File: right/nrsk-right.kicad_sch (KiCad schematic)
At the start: 138 parts, among them J1 USB-C, J2 USB-C, J3 OLED 128x32, SW1 71, SW10 8, SW11 9, SW12 0, SW13 -, SW14 =, SW15 Backspace, SW16 75, SW17 Y, SW18 U, SW19 I, SW2 F7, SW20 O, SW21 P, SW22 [, SW23 ], SW24 \, SW25 77, SW26 H, SW27 J, SW28 K, SW29 L, SW3 F8, SW30 ;, SW31 ', SW32 Enter, SW33 79, SW34 N, SW35 M, SW36 ,, SW37 ., SW38 /, SW39 ↑, SW4 F9, SW40 fn, SW41 81, SW42 Space, SW43 Space, SW44 Cmd, SW45 Opt, SW46 ←, SW47 ↓, SW48 →, SW5 F10, SW6 F11, SW7 F12, SW8 73, SW9 7, U1 RP2040, U2 USBLC6-2SC6, U4 AP2112K-3.3, U5 W25Q128JVS, Y1 12MHz

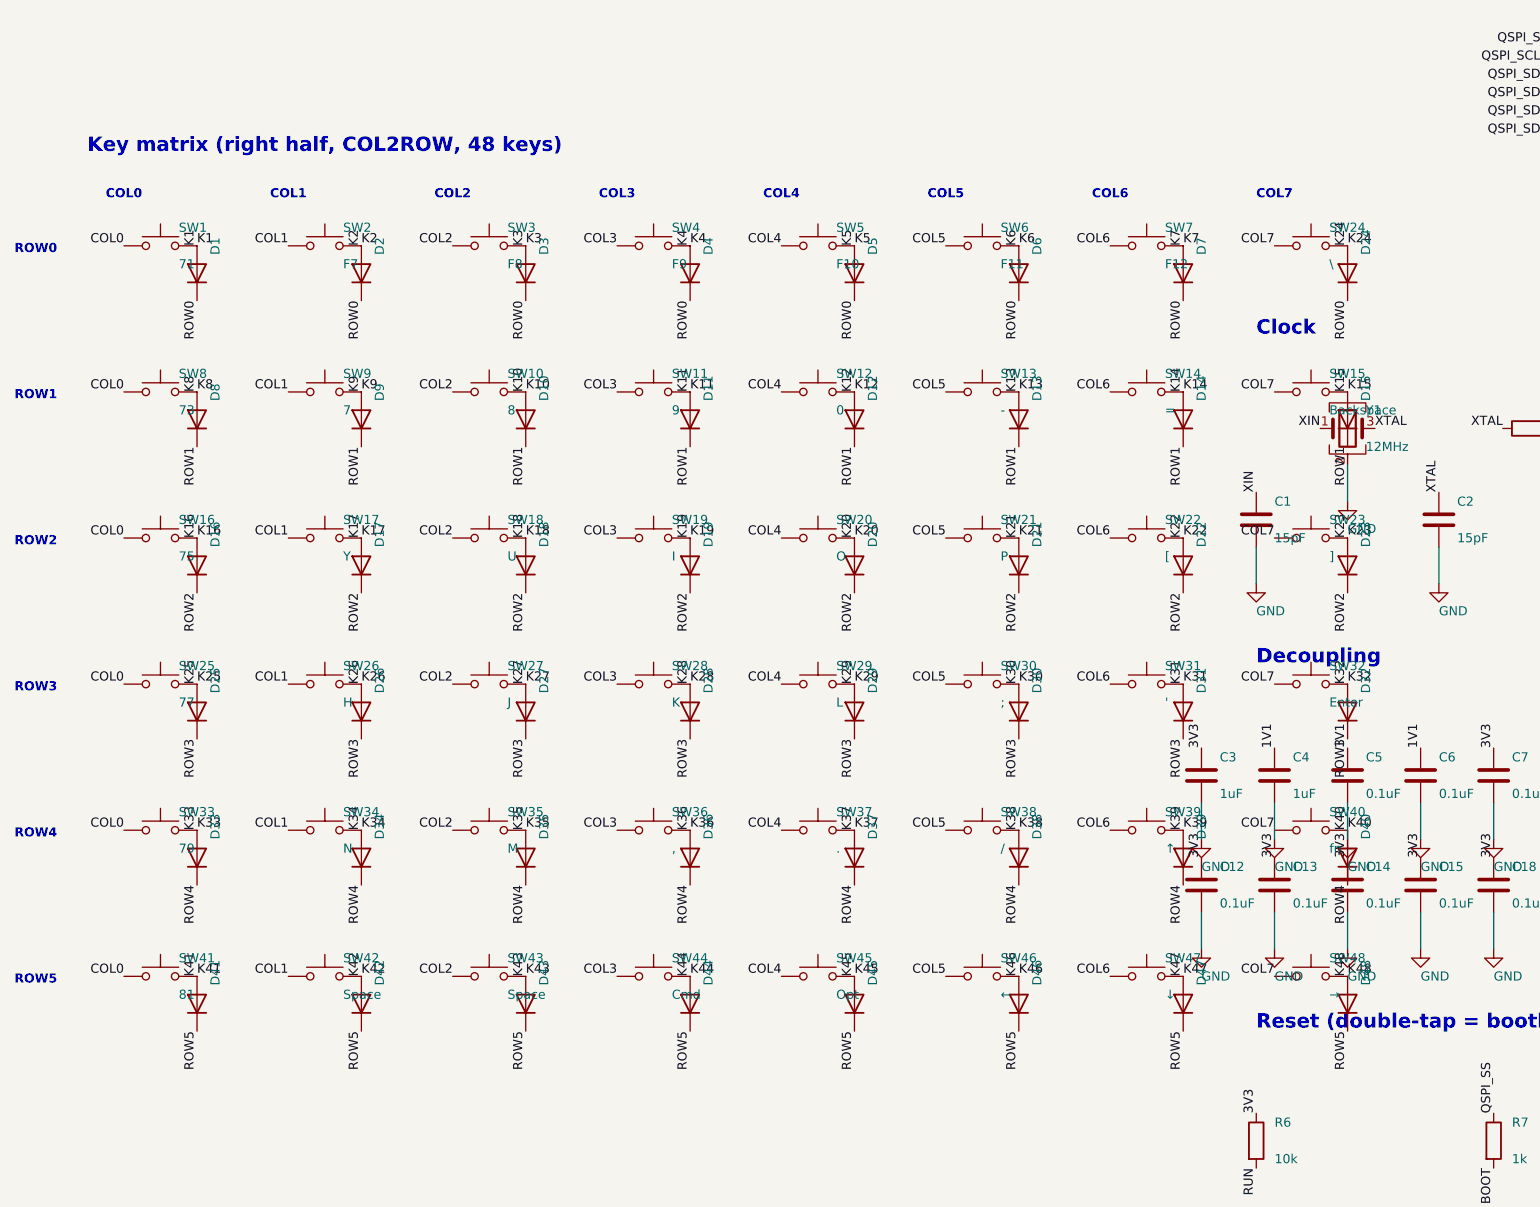
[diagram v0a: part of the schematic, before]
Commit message: Remove the blank inner key column on both halves; even plate band round the OLED cover
KLE: the unlabeled keys of the inner column go (left 8, 16, 23, 30, 37, 44; right 71, 73, 75, 77, 79, 81), so
the halves have 38 + 42 = 80 keys. The right "\" key now sits in its own row (row 2, col 7) and the remap goes;
the left's COL7 stays unconnected in the schematic.

The gap is closed: the right board moves its keys one unit in (key_shift +1 u, width -1 u). The left board is
sized from its row 0-1 keycaps: COVER_FRAME + the OLED cover (window + 5 mm each side) + COVER_FRAME, less the
case wall, so it narrows by 15.4 mm instead of a full unit.

The OLED's half-mirror cover is now laid out from the plate band round it: 3.5 mm to the case outline (top and
inner edge), to the nearest row 0-1 keycaps, and to the row-2 keycap line below, on both halves; the corner at the
case corner is concentric with it (R9), the others R2. The OLED stays at its height: its display glass, 3 mm
toward the module's top, lands at the cover's centre, and higher up the module would leave the board's rounded
corner and meet the link USB-C's shield pins. make_case checks the band against keycaps and the outline.

Sizes: boards 157.1 / 180.5 x 126.3 mm, cases 174.1 / 197.5 x 143.3 mm. The drum stays centred on Backspace.
Docs (README, ordering, pre-order checklist, drum spec coordinates) follow: 80 switches / sockets / diodes,
69 1 u keycaps, LCSC 85 switches and 90 sockets, trays fit a 220 mm bed.

Checked: ./build.sh -> left 0 unconnected (31 zero-length router stubs removed), right 0 unconnected, 0 parity
issues, ERC 0 / 0; DRC 4 silkscreen-at-board-edge warnings per side, as on main; make_case.py checks ok on both
halves (OLED band, drum dial); make_jlc: left 77, right 81 placements; textlint 0 on the edited docs.

Co-Authored-By: Claude Opus 5.5 <noreply@anthropic.com>
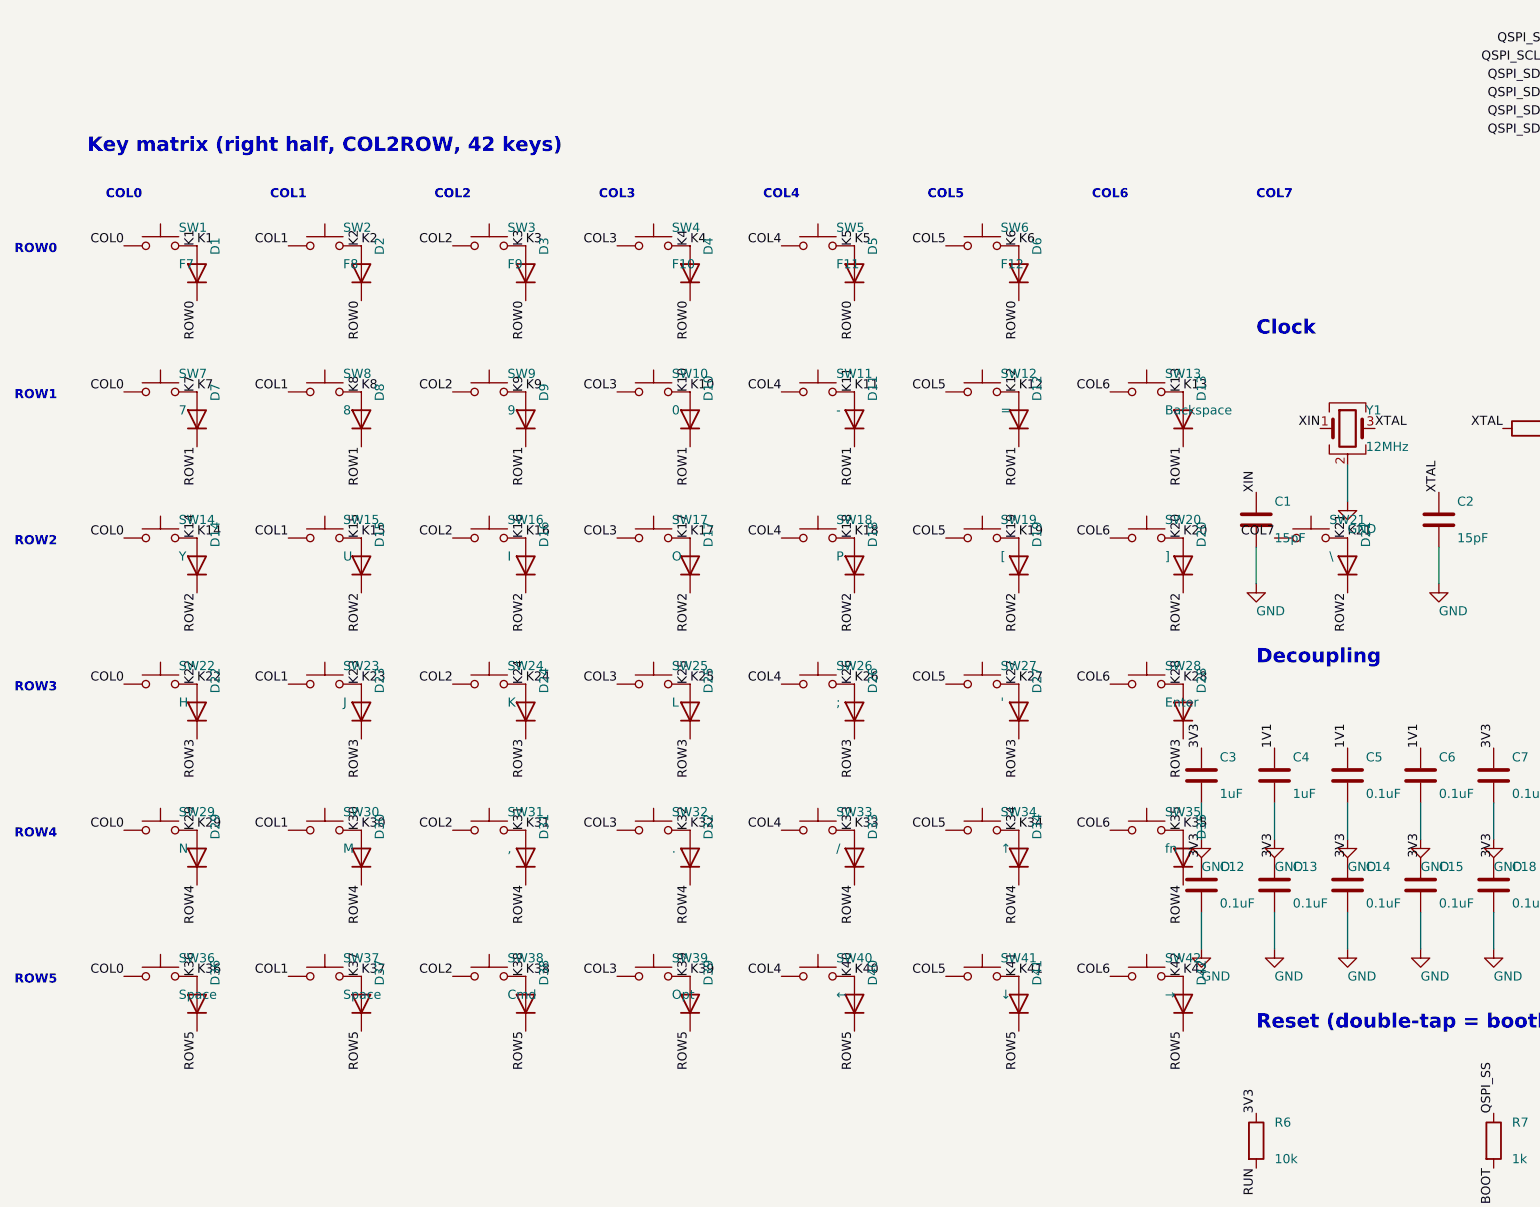
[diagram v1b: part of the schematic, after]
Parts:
- removed D43, D44, D45, D46, D47, D48: 1N4148W, Diode_SMD:D_SOD-123, symbol Device:D
- removed SW43: Space, nrsk:SW_MX_Hotswap_1.00u, symbol Switch:SW_Push
- removed SW44: Cmd, nrsk:SW_MX_Hotswap_1.25u, symbol Switch:SW_Push
- removed SW45: Opt, nrsk:SW_MX_Hotswap_1.25u, symbol Switch:SW_Push
- removed SW46: ←, nrsk:SW_MX_Hotswap_1.00u, symbol Switch:SW_Push
- removed SW47: ↓, nrsk:SW_MX_Hotswap_1.00u, symbol Switch:SW_Push
- removed SW48: →, nrsk:SW_MX_Hotswap_1.00u, symbol Switch:SW_Push
- SW1: value 71 -> F7
- SW10: value 8 -> 0
- SW11: value 9 -> -
- SW12: value 0 -> =
- SW13: value - -> Backspace; footprint nrsk:SW_MX_Hotswap_1.00u -> nrsk:SW_MX_Hotswap_2.00u
- SW14: value = -> Y
- SW15: value Backspace -> U; footprint nrsk:SW_MX_Hotswap_2.00u -> nrsk:SW_MX_Hotswap_1.00u
- SW16: value 75 -> I
- SW17: value Y -> O
- SW18: value U -> P
- SW19: value I -> [
- SW2: value F7 -> F8
- SW20: value O -> ]
- SW21: value P -> \; footprint nrsk:SW_MX_Hotswap_1.00u -> nrsk:SW_MX_Hotswap_1.50u
- SW22: value [ -> H
- SW23: value ] -> J
- SW24: value \ -> K; footprint nrsk:SW_MX_Hotswap_1.50u -> nrsk:SW_MX_Hotswap_1.00u
- SW25: value 77 -> L
- SW26: value H -> ;
- SW27: value J -> '
- SW28: value K -> Enter; footprint nrsk:SW_MX_Hotswap_1.00u -> nrsk:SW_MX_Hotswap_2.25u
- SW29: value L -> N
- SW3: value F8 -> F9
- SW30: value ; -> M
- SW31: value ' -> ,
- SW32: value Enter -> .; footprint nrsk:SW_MX_Hotswap_2.25u -> nrsk:SW_MX_Hotswap_1.00u
- SW33: value 79 -> /
- SW34: value N -> ↑
- SW35: value M -> fn
- SW36: value , -> Space
- SW37: value . -> Space
- SW38: value / -> Cmd; footprint nrsk:SW_MX_Hotswap_1.00u -> nrsk:SW_MX_Hotswap_1.25u
- SW39: value ↑ -> Opt; footprint nrsk:SW_MX_Hotswap_1.00u -> nrsk:SW_MX_Hotswap_1.25u
- SW4: value F9 -> F10
- SW40: value fn -> ←
- SW41: value 81 -> ↓
- SW42: value Space -> →
- SW5: value F10 -> F11
- SW6: value F11 -> F12
- SW7: value F12 -> 7
- SW8: value 73 -> 8
- SW9: value 7 -> 9
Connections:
- net COL0: now also SW14.1, SW22.1, SW29.1, SW36.1, SW7.1; no longer SW16.1, SW25.1, SW33.1, SW41.1, SW8.1
- net COL1: now also SW15.1, SW23.1, SW30.1, SW37.1, SW8.1; no longer SW17.1, SW26.1, SW34.1, SW42.1, SW9.1
- net COL2: now also SW16.1, SW24.1, SW31.1, SW38.1, SW9.1; no longer SW10.1, SW18.1, SW27.1, SW35.1
- net COL3: now also SW10.1, SW17.1, SW25.1, SW32.1, SW39.1; no longer SW11.1, SW19.1, SW28.1, SW36.1
- net COL4: now also SW11.1, SW18.1, SW26.1, SW33.1, SW40.1; no longer SW12.1, SW20.1, SW29.1, SW37.1
- net COL5: now also SW12.1, SW19.1, SW27.1, SW34.1, SW41.1; no longer SW13.1, SW21.1, SW30.1, SW38.1
- net COL6: now also SW13.1, SW20.1, SW28.1, SW35.1, SW42.1; no longer SW14.1, SW22.1, SW31.1, SW39.1, SW7.1
- net GND: no longer D40.2 (A), SW15.1, SW23.1, SW24.1, SW32.1, SW40.1, SW40.2, U1.29 (GPIO18)
- net ROW0: no longer D24.1 (K), D7.1 (K)
- net ROW1: now also D7.1 (K); no longer D14.1 (K), D15.1 (K)
- net ROW2: now also D14.1 (K), D15.1 (K); no longer D22.1 (K), D23.1 (K)
- net ROW3: now also D22.1 (K), D23.1 (K), D24.1 (K); no longer D29.1 (K), D30.1 (K), D31.1 (K), D32.1 (K)
- net ROW4: now also D29.1 (K), D30.1 (K), D31.1 (K), D32.1 (K); no longer D36.1 (K), D37.1 (K), D38.1 (K), D39.1 (K), D40.1 (K)
- net ROW5: now also D36.1 (K), D37.1 (K), D38.1 (K), D39.1 (K), D40.1 (K)
- new net COL7: SW21.1, U1.29 (GPIO18)
- new net K40: D40.2 (A), SW40.2
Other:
- note added: "Key matrix (right half, COL2ROW, 42 keys)"
- note removed: "Key matrix (right half, COL2ROW, 48 keys)"
- moved on the sheet: D10, D11, D12, D13, D14, D15, D16, D17, D18, D19, D20, D21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

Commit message: Move the RP2040 and its support parts to the front, visible through the clear plate
- RP2040, flash, crystal, LDO, decoupling caps and resistors on the front, in the
  key-free strip along the inner edge (clear of every keycap and the OLED cover);
  USB-C and its protection parts, reset switch and BOOTSEL pad stay on the back
- RP2040 fixed with pin 1 top-left so its Raspberry Pi logo reads upright
  (datasheet Figure 168); make_pcb asserts the orientation
- Left half: pin row 1-14 faces the keys, so it is fanned out to 1 mm pitch and
  the matrix rows are routed by make_pcb; Freerouting does the rest
- build.sh retries routing until 0 unconnected and 0 DRC violations
- USB-C footprint copy in lib/nrsk.pretty with its outline on Fab (no clipped silk)
- JLC CPL handles top-side parts; front assembly drawing added
- Printed plate B: web cut away over the front-side parts
- DRC (all severities) 0, unconnected 0, parity 0, ERC 0 on both halves
- Docs, renders, fab outputs and case files regenerated

Co-Authored-By: Claude Opus 5.5 <noreply@anthropic.com>
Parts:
- J1, J2: footprint Connector_USB:USB_C_Receptacle_HRO_TYPE-C-31-M-12 -> nrsk:USB_C_Receptacle_HRO_TYPE-C-31-M-12
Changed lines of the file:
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@@
 	  (property "Reference" "J2" (at 345.44 58.42 0) (effects (font (size 1.27 1.27)) (justify left)))
 	  (property "Value" "USB-C" (at 345.44 63.50 0) (effects (font (size 1.27 1.27)) (justify left)))
-	  (property "Footprint" "Connector_USB:USB_C_Receptacle_HRO_TYPE-C-31-M-12" (at 342.90 60.96 0) (effects (font (size 1.27 1.27)) (hide yes)))
+	  (property "Footprint" "nrsk:USB_C_Receptacle_HRO_TYPE-C-31-M-12" (at 342.90 60.96 0) (effects (font (size 1.27 1.27)) (hide yes)))
 	  (property "Datasheet" "" (at 342.90 60.96 0) (effects (font (size 1.27 1.27)) (hide yes)))
 	  (pin "A1")
@@
 	  (property "Reference" "J1" (at 345.44 165.10 0) (effects (font (size 1.27 1.27)) (justify left)))
 	  (property "Value" "USB-C" (at 345.44 170.18 0) (effects (font (size 1.27 1.27)) (justify left)))
-	  (property "Footprint" "Connector_USB:USB_C_Receptacle_HRO_TYPE-C-31-M-12" (at 342.90 167.64 0) (effects (font (size 1.27 1.27)) (hide yes)))
+	  (property "Footprint" "nrsk:USB_C_Receptacle_HRO_TYPE-C-31-M-12" (at 342.90 167.64 0) (effects (font (size 1.27 1.27)) (hide yes)))
 	  (property "Datasheet" "" (at 342.90 167.64 0) (effects (font (size 1.27 1.27)) (hide yes)))
 	  (pin "A1")
